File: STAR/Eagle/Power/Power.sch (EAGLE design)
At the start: 51 parts, among them J1 J30J-25, U1 LMR16020, U2 LMR16020, U3 LMR16020

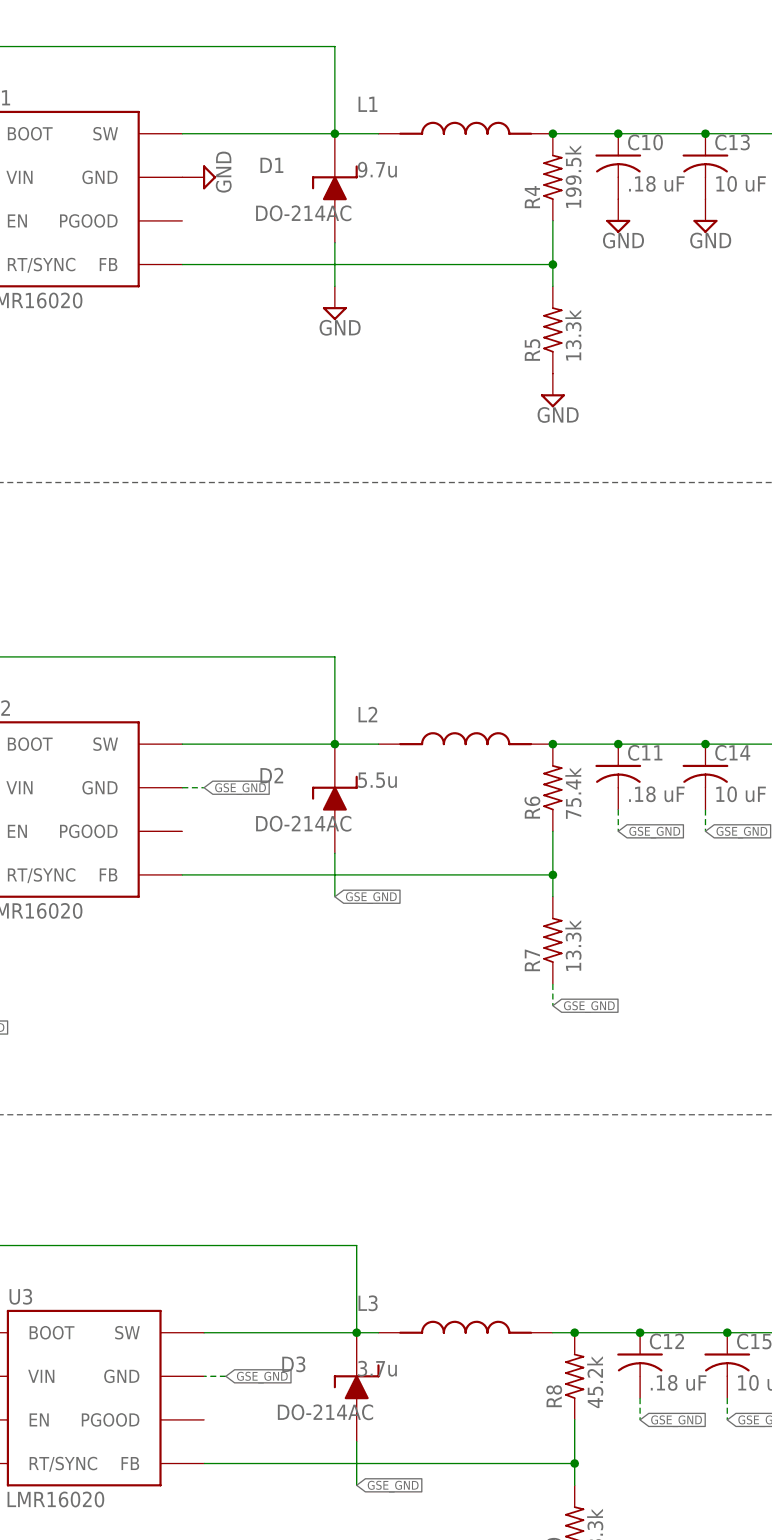
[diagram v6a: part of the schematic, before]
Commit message: New inductors for the power board, changed the error message on the values script and added CBEs. Because who needs sleep
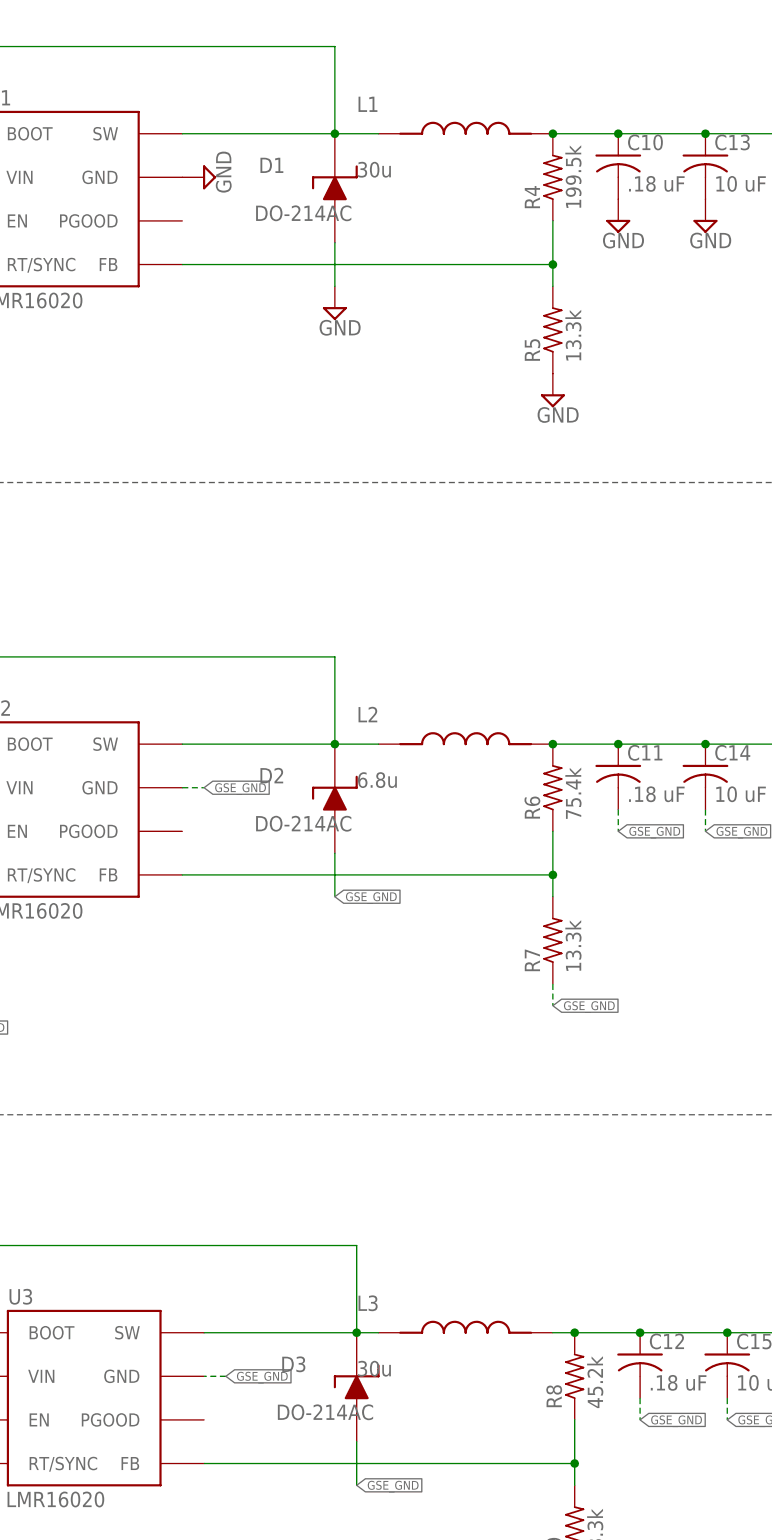
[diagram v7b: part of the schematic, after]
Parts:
- L1: value 9.7u -> 30u; device Power:744314101 -> Filtering:744314101
- L2: value 5.5u -> 6.8u; device Filtering:744325550 -> Filtering:744314101
- L3: value 3.7u -> 30u; device Power:7443551370 -> Filtering:7443551370
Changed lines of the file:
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@@
 <?xml version="1.0" encoding="utf-8"?>
 <!DOCTYPE eagle SYSTEM "eagle.dtd">
-<eagle version="9.1.0">
+<eagle version="7.6.0">
 <drawing>
 <settings>
 <setting alwaysvectorfont="no"/>
-<setting keepoldvectorfont="yes"/>
 <setting verticaltext="up"/>
 </settings>
@@
 <part name="C11" library="resistor" deviceset="C-US" device="C0603" value=".18 uF"/>
 <part name="R6" library="resistor" deviceset="R-US_" device="R0603" value="75.4k"/>
-<part name="L2" library="Filtering" deviceset="744325550" device="" value="5.5u"/>
-<part name="L3" library="Power" deviceset="7443551370" device="" value="3.7u"/>
+<part name="L2" library="Filtering" deviceset="744314101" device="" value="6.8u"/>
+<part name="L3" library="Filtering" deviceset="7443551370" device="" value="30u"/>
 <part name="C7" library="resistor" deviceset="C-US" device="C0603" value=".1 uF"/>
 <part name="SUPPLY1" library="supply2" deviceset="GND" device=""/>
@@
 <part name="C10" library="resistor" deviceset="C-US" device="C0603" value=".18 uF"/>
 <part name="R4" library="resistor" deviceset="R-US_" device="R0603" value="199.5k"/>
-<part name="L1" library="Power" deviceset="744314101" device="" value="9.7u"/>
+<part name="L1" library="Filtering" deviceset="744314101" device="" value="30u"/>
 <part name="U$1" library="Filtering" deviceset="DFT7160-105B" device=""/>
 <part name="L4" library="Filtering" deviceset="744029000068" device=""/>

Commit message: gerbers
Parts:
- removed C17, C19, C21, C23, C25: 1nF, resistor:C-USC0603
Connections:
- new net N$38: U$1.P$4
- net 12V_FILT: no longer C25.1
- net 3V3_FILT: no longer C21.1
- net 5V_FILT: no longer C19.1
- net GND: no longer C23.2, C25.2
- net GSE_FILT: now also L4.P$2; no longer C17.1, U$3.P$1
- net GSE_GND: no longer C17.2, C19.2, C21.2, U$1.P$2
- net GSE_GND_IN: now also J1.15, U$1.P$3; no longer J1.14, U$1.P$1
- net GSE_UFILT: now also J1.14, U$1.P$1; no longer J1.15, U$1.P$3
- net N$28: now also U$3.P$1; no longer U$1.P$4
- net N$29: now also U$6.P$1; no longer L7.P$1
- net N$31: now also U$1.P$2; no longer L4.P$2
- net N$34: now also L7.P$1, U$6.P$2; no longer L7.P$2, U$6.P$1
- net TE_FILT: now also L7.P$2; no longer C23.1, U$6.P$2
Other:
- moved on the sheet: L4, L7, U$1
